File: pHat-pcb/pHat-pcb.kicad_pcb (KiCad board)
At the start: 2 copper layers, 65 x 30 mm, 22 parts, among them J1 Conn_02x20_Odd_Even, J2 Conn_01x24_Male, J3 Conn_Active_High, J4 Conn_Bat, J5 Conn_I2C, J6 Conn_01x04_Male, J8 Conn_Active_Low, SW1 SW_Push, SW2 SW_Push, U1 TPS61023_Breakout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

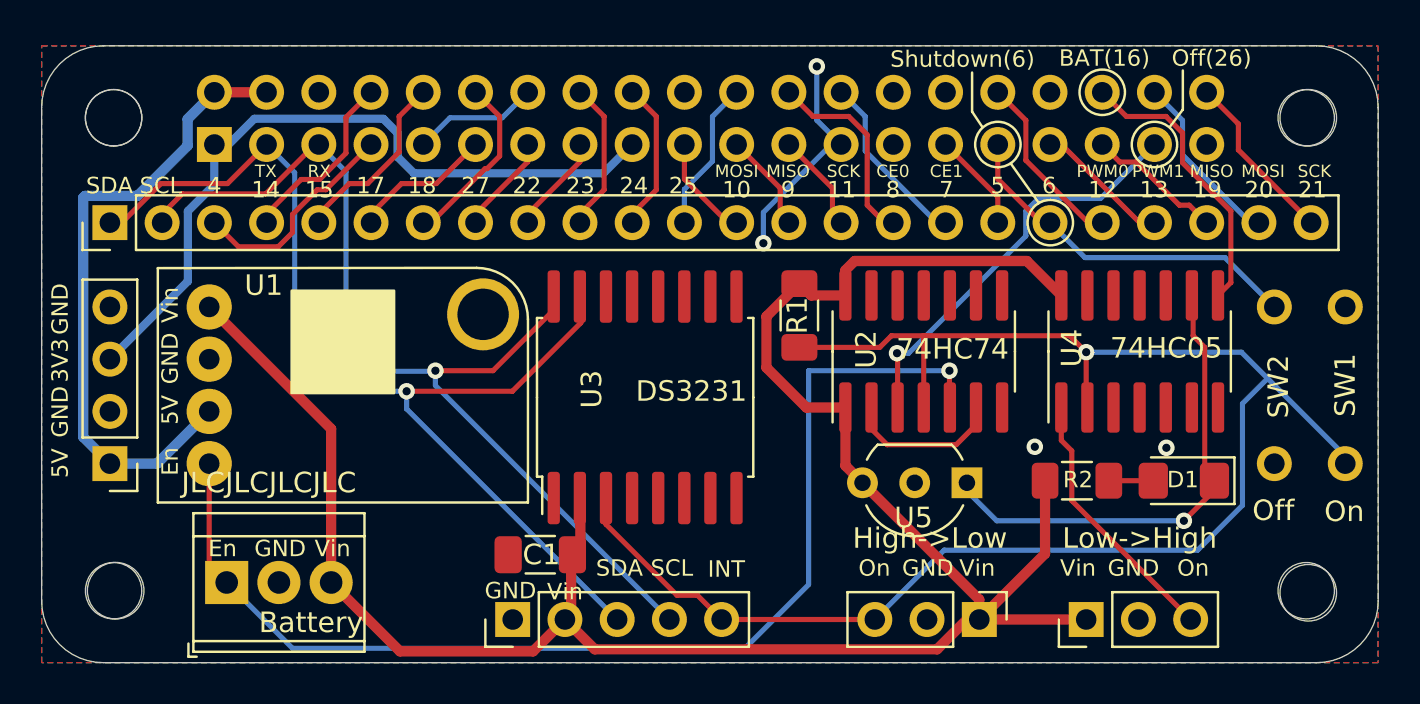
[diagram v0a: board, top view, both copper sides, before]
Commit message: Rev8: add 5V to external battery connector / fixed KA75330 pin-order / updated labels
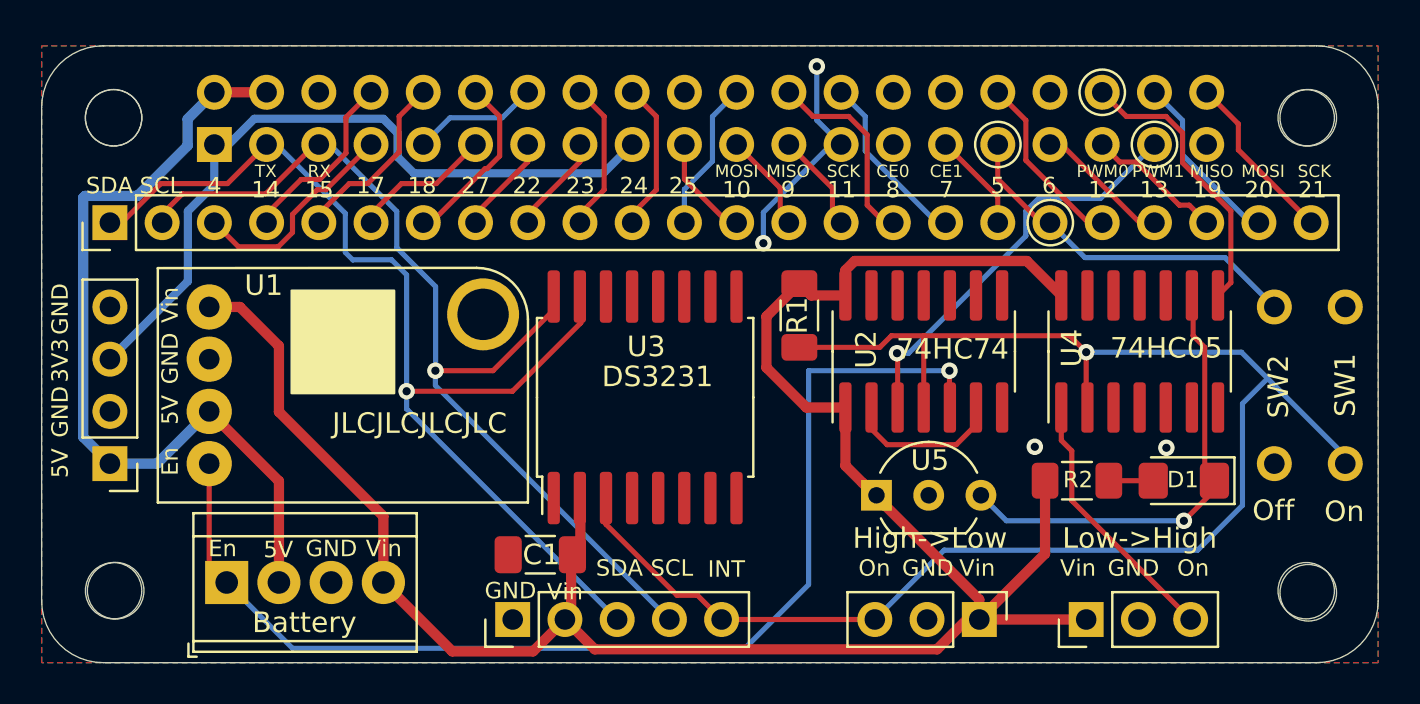
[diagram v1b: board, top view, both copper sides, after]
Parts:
- J4: footprint TerminalBlock_TE-Connectivity:TerminalBlock_TE_282834-3_1x03_P2.54mm_Horizontal -> TerminalBlock_TE-Connectivity:TerminalBlock_TE_282834-4_1x04_P2.54mm_Horizontal
- moved U5 4.44 mm to (90.6, 70.9), turned to 0 degrees
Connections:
- J4 pad 2: GND -> +5V
- J4 pad 3: /Vin -> GND
- U5 pad 1: /BatOk -> /Vin
- U5 pad 3: /Vin -> /BatOk
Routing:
- net +5V: track 31.2 -> 40.9 mm
- net /GPIO3(SCL1): track 49.0 -> 47.8 mm
- net /BatOk: track 23.7 -> 22.5 mm
- net /Vin: track 107.9 -> 107.3 mm
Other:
- board text added: "GPIO6: dtoverlay=gpio-shutdown,gpio_pin=6 GPIO16: low battery (low->high) GPIO26: dtoverlay=gpio-poweroff"
- board text added: "Rev 8"
- board text removed: "BAT(16)"
- board text removed: "Off(26)"
- board text removed: "Rev 7"
- board text removed: "Shutdown(6)"

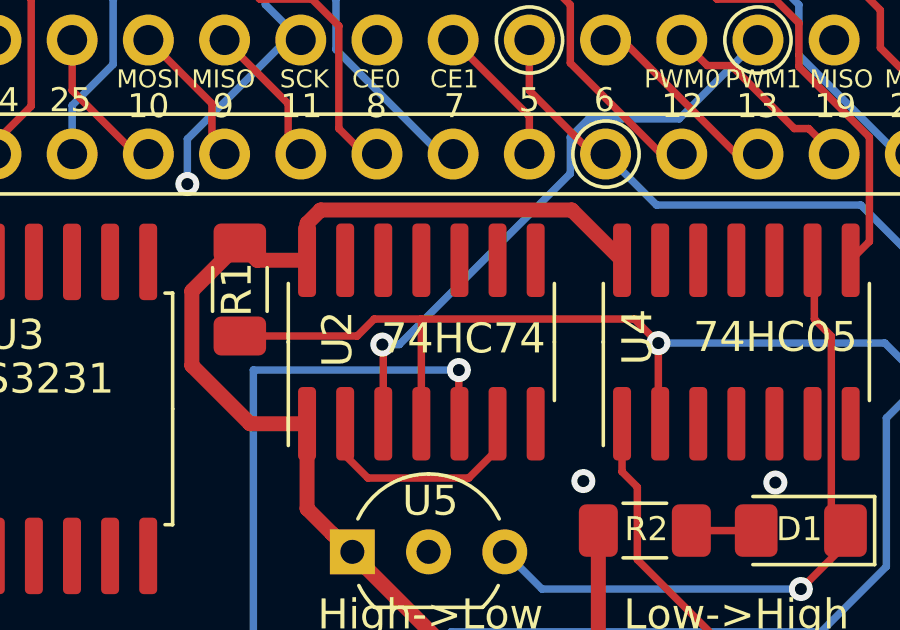
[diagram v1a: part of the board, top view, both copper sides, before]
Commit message: bugfix: prevent 2nd flip-flop from floating
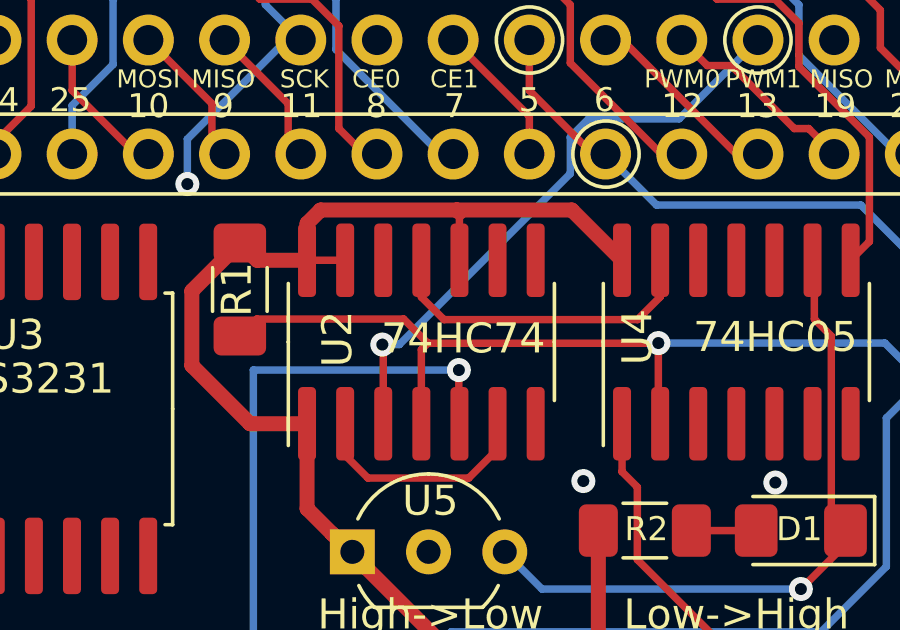
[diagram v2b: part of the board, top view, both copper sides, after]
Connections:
- U2 pad 10: Net-(U2-Pad10) -> /Vin
- U2 pad 11: Net-(U2-Pad11) -> GND
- U2 pad 12: Net-(U2-Pad12) -> GND
- U2 pad 13: Net-(U2-Pad13) -> /Vin
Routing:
- net GND: track 17.1 -> 28.1 mm
- net /Vin: track 107.3 -> 110.3 mm
- net /1~PRE: track 81.3 -> 80.6 mm
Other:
- board text added: "Rev 9"
- board text removed: "Rev 8"
